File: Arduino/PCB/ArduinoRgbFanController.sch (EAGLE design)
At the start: 60 parts, among them IC2 ARDUINO_MKRFOX1200PROTOPADS, Q1 IRLML9301TRPBF, Q2 2N7002, Q3 2N7002, Q4 IRLML9301TRPBF

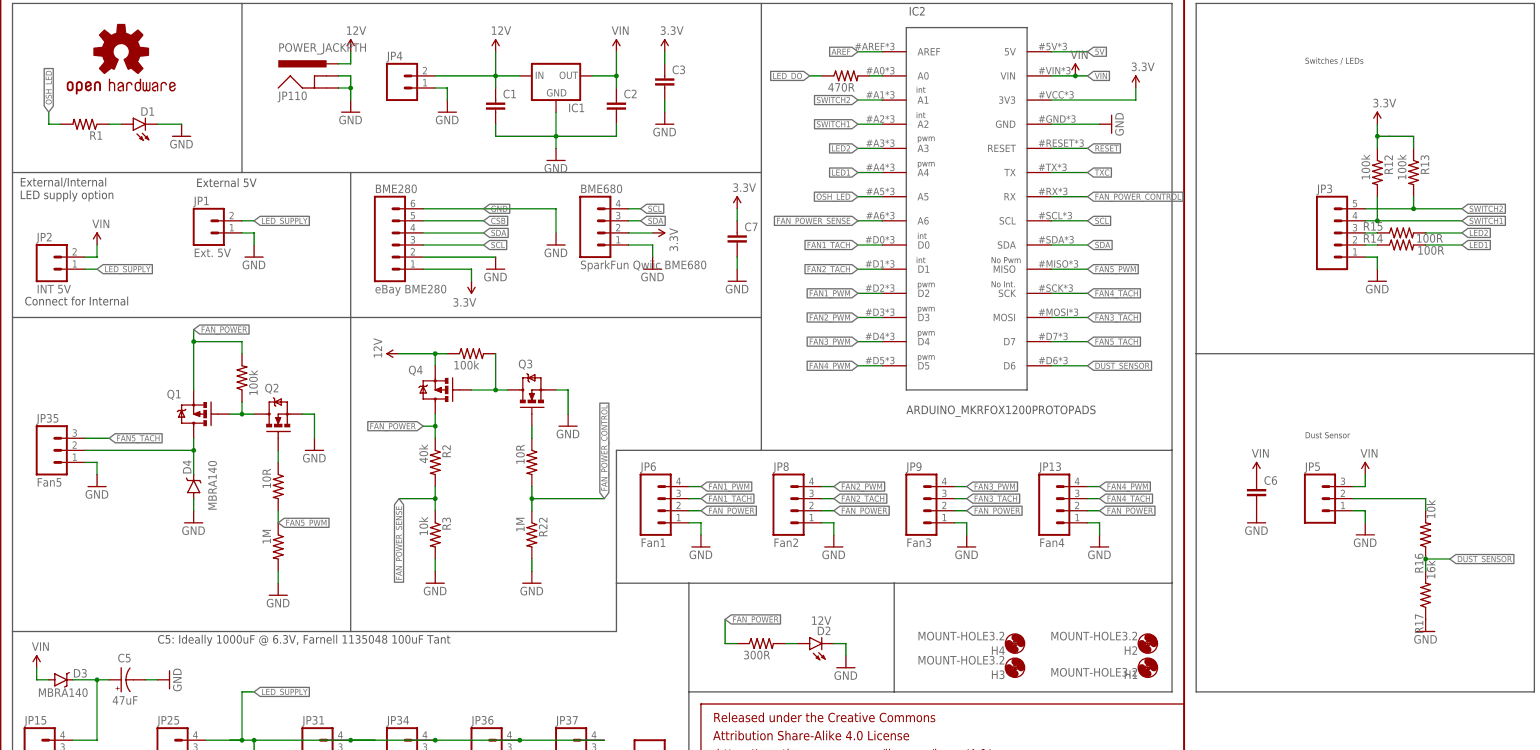
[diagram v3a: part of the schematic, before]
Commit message: Updated component values whilst building boards.
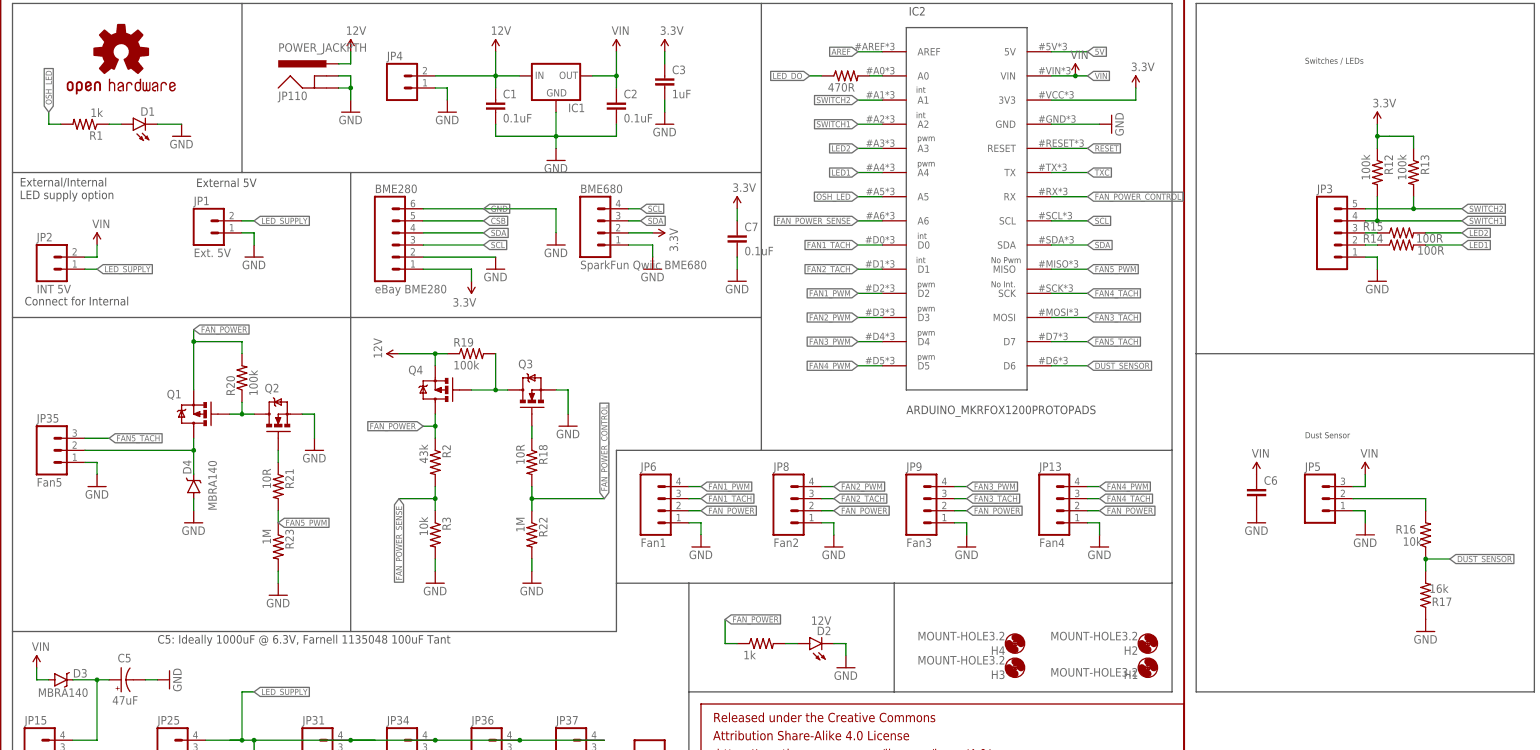
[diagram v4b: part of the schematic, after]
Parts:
- C1, C2, C7: value (none) -> 0.1uF
- C3: value (none) -> 1uF
- JP6: FARNELL (none) -> 2313705; MOLEX (none) -> 47053-1000
- Q1, Q4: value IRLML9301TRPBF -> IRLML930; FARNELL (none) -> 1831089
- Q2, Q3: FARNELL (none) -> 1510761
- R1: value (none) -> 1k
- R2: value 40k -> 43k
- R28: value 300R -> 1k
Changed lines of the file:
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@@
 <part name="FRAME1" library="SparkFun-Aesthetics" deviceset="FRAME-LETTER" device=""/>
 <part name="IC1" library="v-reg" deviceset="78XXS" device=""/>
-<part name="C1" library="SparkFun-Capacitors" deviceset="1UF-25V-10%(0805)" device="&quot;"/>
-<part name="C2" library="SparkFun-Capacitors" deviceset="1UF-25V-10%(0805)" device="&quot;"/>
+<part name="C1" library="SparkFun-Capacitors" deviceset="1UF-25V-10%(0805)" device="&quot;" value="0.1uF"/>
+<part name="C2" library="SparkFun-Capacitors" deviceset="1UF-25V-10%(0805)" device="&quot;" value="0.1uF"/>
 <part name="H1" library="holes" deviceset="MOUNT-HOLE" device="3.2"/>
 <part name="H2" library="holes" deviceset="MOUNT-HOLE" device="3.2"/>
@@
 <part name="H4" library="holes" deviceset="MOUNT-HOLE" device="3.2"/>
 <part name="D1" library="SparkFun-LED" deviceset="LED" device="1206-BOTTOM"/>
-<part name="R1" library="SparkFun-Resistors" deviceset="RESISTOR" device="0805-RES"/>
+<part name="R1" library="SparkFun-Resistors" deviceset="RESISTOR" device="0805-RES" value="1k"/>
 <part name="GND1" library="SparkFun-Aesthetics" deviceset="GND" device=""/>
 <part name="GND3" library="SparkFun-Aesthetics" deviceset="GND" device=""/>
@@
 <part name="SUPPLY12" library="SparkFun-Aesthetics" deviceset="12V" device=""/>
 <part name="GND11" library="SparkFun-Aesthetics" deviceset="GND" device=""/>
-<part name="C3" library="SparkFun-Capacitors" deviceset="1UF-25V-10%(0805)" device="&quot;"/>
+<part name="C3" library="SparkFun-Capacitors" deviceset="1UF-25V-10%(0805)" device="&quot;" value="1uF"/>
 <part name="SUPPLY14" library="SparkFun-Aesthetics" deviceset="3.3V" device=""/>
 <part name="GND12" library="SparkFun-Aesthetics" deviceset="GND" device=""/>
 <part name="LOGO3" library="SparkFun-Aesthetics" deviceset="OSHW-LOGO" device="M"/>
-<part name="C7" library="SparkFun-Capacitors" deviceset="1UF-25V-10%(0805)" device="&quot;"/>
+<part name="C7" library="SparkFun-Capacitors" deviceset="1UF-25V-10%(0805)" device="&quot;" value="0.1uF"/>
 <part name="SUPPLY17" library="SparkFun-Aesthetics" deviceset="3.3V" device=""/>
 <part name="GND15" library="SparkFun-Aesthetics" deviceset="GND" device=""/>
@@
 <part name="SUPPLY18" library="SparkFun-Aesthetics" deviceset="3.3V" device=""/>
 <part name="GND16" library="SparkFun-Aesthetics" deviceset="GND" device=""/>
-<part name="R28" library="SparkFun-Resistors" deviceset="RESISTOR" device="1206" value="300R"/>
+<part name="R28" library="SparkFun-Resistors" deviceset="RESISTOR" device="1206" value="1k"/>
 <part name="D2" library="SparkFun-LED" deviceset="LED-RED" device="1206" value="12V"/>
 <part name="GND2" library="SparkFun-Aesthetics" deviceset="GND" device=""/>
-<part name="JP6" library="SparkFun-Connectors" deviceset="M04" device="POLAR" value="Fan1"/>
+<part name="JP6" library="SparkFun-Connectors" deviceset="M04" device="POLAR" value="Fan1">
+<attribute name="FARNELL" value="2313705"/>
+<attribute name="MOLEX" value="47053-1000"/>
+</part>
 <part name="JP8" library="SparkFun-Connectors" deviceset="M04" device="POLAR" value="Fan2"/>
 <part name="JP9" library="SparkFun-Connectors" deviceset="M04" device="POLAR" value="Fan3"/>
@@
 <part name="GND21" library="SparkFun-Aesthetics" deviceset="GND" device=""/>
 <part name="GND22" library="SparkFun-Aesthetics" deviceset="GND" device=""/>
-<part name="Q1" library="SparkFun-DiscreteSemi" deviceset="MOSFET-PCHANNEL" device="" value="IRLML9301TRPBF"/>
-<part name="Q2" library="SparkFun-DiscreteSemi" deviceset="MOSFET-NCHANNEL" device="AO3404A" value="2N7002"/>
+<part name="Q1" library="SparkFun-DiscreteSemi" deviceset="MOSFET-PCHANNEL" device="" value="IRLML930">
+<attribute name="FARNELL" value="1831089"/>
+</part>
+<part name="Q2" library="SparkFun-DiscreteSemi" deviceset="MOSFET-NCHANNEL" device="AO3404A" value="2N7002">
+<attribute name="FARNELL" value="1510761"/>
+</part>
 <part name="R20" library="SparkFun-Resistors" deviceset="RESISTOR" device="0805-RES" value="100k"/>
 <part name="R21" library="SparkFun-Resistors" deviceset="RESISTOR" device="0805-RES" value="10R"/>
@@
 <part name="SUPPLY24" library="SparkFun-Aesthetics" deviceset="VIN" device=""/>
 <part name="SUPPLY25" library="SparkFun-Aesthetics" deviceset="VIN" device=""/>
-<part name="Q3" library="SparkFun-DiscreteSemi" deviceset="MOSFET-NCHANNEL" device="AO3404A" value="2N7002"/>
+<part name="Q3" library="SparkFun-DiscreteSemi" deviceset="MOSFET-NCHANNEL" device="AO3404A" value="2N7002">
+<attribute name="FARNELL" value="1510761"/>
+</part>
 <part name="R18" library="SparkFun-Resistors" deviceset="RESISTOR" device="0805-RES" value="10R"/>
-<part name="Q4" library="SparkFun-DiscreteSemi" deviceset="MOSFET-PCHANNEL" device="" value="IRLML9301TRPBF"/>
+<part name="Q4" library="SparkFun-DiscreteSemi" deviceset="MOSFET-PCHANNEL" device="" value="IRLML930">
+<attribute name="FARNELL" value="1831089"/>
+</part>
 <part name="R19" library="SparkFun-Resistors" deviceset="RESISTOR" device="0805-RES" value="100k"/>
 <part name="SUPPLY26" library="SparkFun-Aesthetics" deviceset="12V" device=""/>
@@
 <part name="SUPPLY2" library="SparkFun-Aesthetics" deviceset="VIN" device=""/>
 <part name="GND6" library="SparkFun-Aesthetics" deviceset="GND" device=""/>
-<part name="R2" library="SparkFun-Resistors" deviceset="RESISTOR" device="0805-RES" value="40k"/>
+<part name="R2" library="SparkFun-Resistors" deviceset="RESISTOR" device="0805-RES" value="43k"/>
 <part name="R3" library="SparkFun-Resistors" deviceset="RESISTOR" device="0805-RES" value="10k"/>
 <part name="GND7" library="SparkFun-Aesthetics" deviceset="GND" device=""/>
@@
 <instance part="D2" gate="G$1" x="170.18" y="48.26" rot="R90"/>
 <instance part="GND2" gate="1" x="177.8" y="43.18"/>
-<instance part="JP6" gate="G$1" x="139.7" y="76.2"/>
+<instance part="JP6" gate="G$1" x="139.7" y="76.2">
+<attribute name="FARNELL" x="139.7" y="76.2" size="1.778" layer="96" display="off"/>
+<attribute name="MOLEX" x="139.7" y="76.2" size="1.778" layer="96" display="off"/>
+</instance>
 <instance part="JP8" gate="G$1" x="167.64" y="76.2"/>
 <instance part="JP9" gate="G$1" x="195.58" y="76.2"/>
@@
 <instance part="Q1" gate="G$1" x="40.64" y="96.52" smashed="yes" rot="R180">
 <attribute name="NAME" x="38.1" y="101.6" size="1.778" layer="95" rot="R180"/>
+<attribute name="FARNELL" x="40.64" y="96.52" size="1.778" layer="96" rot="R180" display="off"/>
 </instance>
 <instance part="Q2" gate="G$1" x="58.42" y="96.52" smashed="yes" rot="R90">
 <attribute name="NAME" x="58.674" y="102.87" size="1.778" layer="95" rot="R180"/>
-</instance>
-<instance part="R20" gate="G$1" x="50.8" y="104.14" smashed="yes" rot="R90">
-<attribute name="VALUE" x="54.102" y="100.33" size="1.778" layer="96" rot="R90"/>
-</instance>
-<instance part="R21" gate="G$1" x="58.42" y="81.28" smashed="yes" rot="R270">
-<attribute name="VALUE" x="55.118" y="85.09" size="1.778" layer="96" rot="R270"/>
-</instance>
+<attribute name="FARNELL" x="58.42" y="96.52" size="1.778" layer="96" rot="R90" display="off"/>
+</instance>
+<instance part="R20" gate="G$1" x="50.8" y="104.14" rot="R90"/>
+<instance part="R21" gate="G$1" x="58.42" y="81.28" rot="R270"/>
 <instance part="GND23" gate="1" x="20.32" y="81.28"/>
 <instance part="GND24" gate="1" x="66.04" y="88.9"/>
@@
 <instance part="JP5" gate="G$1" x="276.86" y="78.74"/>
 <instance part="R16" gate="G$1" x="299.72" y="71.12" smashed="yes" rot="R90">
-<attribute name="NAME" x="299.2374" y="62.992" size="1.778" layer="95" rot="R90"/>
-<attribute name="VALUE" x="301.752" y="74.422" size="1.778" layer="96" rot="R90"/>
+<attribute name="NAME" x="297.688" y="73.1774" size="1.778" layer="95" rot="R180"/>
+<attribute name="VALUE" x="298.958" y="70.612" size="1.778" layer="96" rot="R180"/>
 </instance>
 <instance part="R17" gate="G$1" x="299.72" y="58.42" smashed="yes" rot="R90">
-<attribute name="NAME" x="299.2374" y="50.292" size="1.778" layer="95" rot="R90"/>
-<attribute name="VALUE" x="301.752" y="61.722" size="1.778" layer="96" rot="R90"/>
+<attribute name="NAME" x="305.308" y="57.9374" size="1.778" layer="95" rot="R180"/>
+<attribute name="VALUE" x="300.482" y="58.928" size="1.778" layer="96"/>
 </instance>
 <instance part="GND34" gate="1" x="287.02" y="71.12"/>
@@
 <instance part="Q3" gate="G$1" x="111.76" y="101.6" smashed="yes" rot="R90">
 <attribute name="NAME" x="112.014" y="107.95" size="1.778" layer="95" rot="R180"/>
-</instance>
-<instance part="R18" gate="G$1" x="111.76" y="86.36" smashed="yes" rot="R270">
-<attribute name="VALUE" x="108.458" y="90.17" size="1.778" layer="96" rot="R270"/>
-</instance>
+<attribute name="FARNELL" x="111.76" y="101.6" size="1.778" layer="96" rot="R90" display="off"/>
+</instance>
+<instance part="R18" gate="G$1" x="111.76" y="86.36" rot="R270"/>
 <instance part="Q4" gate="G$1" x="91.44" y="101.6" smashed="yes" rot="R180">
 <attribute name="NAME" x="88.9" y="106.68" size="1.778" layer="95" rot="R180"/>
-</instance>
-<instance part="R19" gate="G$1" x="99.06" y="109.22" smashed="yes">
-<attribute name="VALUE" x="95.25" y="105.918" size="1.778" layer="96"/>
-</instance>
+<attribute name="FARNELL" x="91.44" y="101.6" size="1.778" layer="96" rot="R180" display="off"/>
+</instance>
+<instance part="R19" gate="G$1" x="99.06" y="109.22"/>
 <instance part="SUPPLY26" gate="G$1" x="83.82" y="109.22" rot="R90"/>
 <instance part="GND36" gate="1" x="119.38" y="93.98"/>
@@
 </instance>
 <instance part="GND37" gate="1" x="111.76" y="60.96"/>
-<instance part="R23" gate="G$1" x="58.42" y="68.58" smashed="yes" rot="R270">
-<attribute name="VALUE" x="55.118" y="72.39" size="1.778" layer="96" rot="R270"/>
-</instance>
+<instance part="R23" gate="G$1" x="58.42" y="68.58" rot="R270"/>
 <instance part="GND38" gate="1" x="58.42" y="58.42"/>
 <instance part="C6" gate="G$1" x="264.16" y="78.74"/>
